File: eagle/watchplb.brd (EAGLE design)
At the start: 100 x 80 mm, 99 parts, among them IC1 SAM-M8Q, IC2 BM70BLES1FC2-0B03AA, Q1 8MHz / LFXTAL020423Reel, Q3 DMN3023L-7, U1 MCP111-XXXXX/TO, U2 STM32L073RZ, U3 MCP2200-I/SS

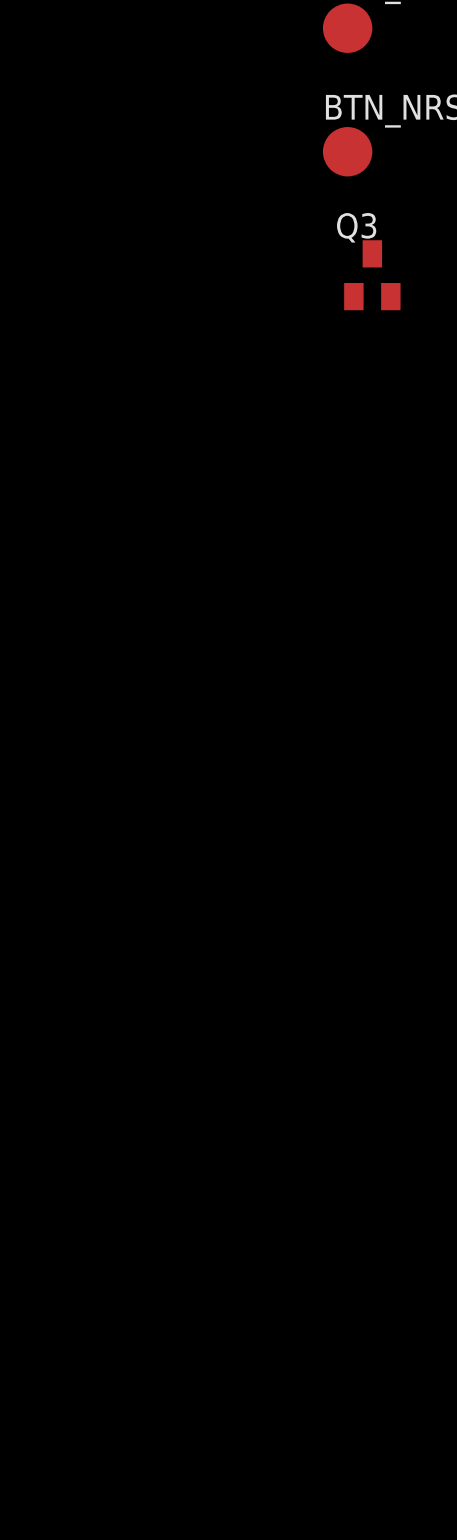
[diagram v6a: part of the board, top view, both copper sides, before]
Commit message: added VCOM usb port with protection
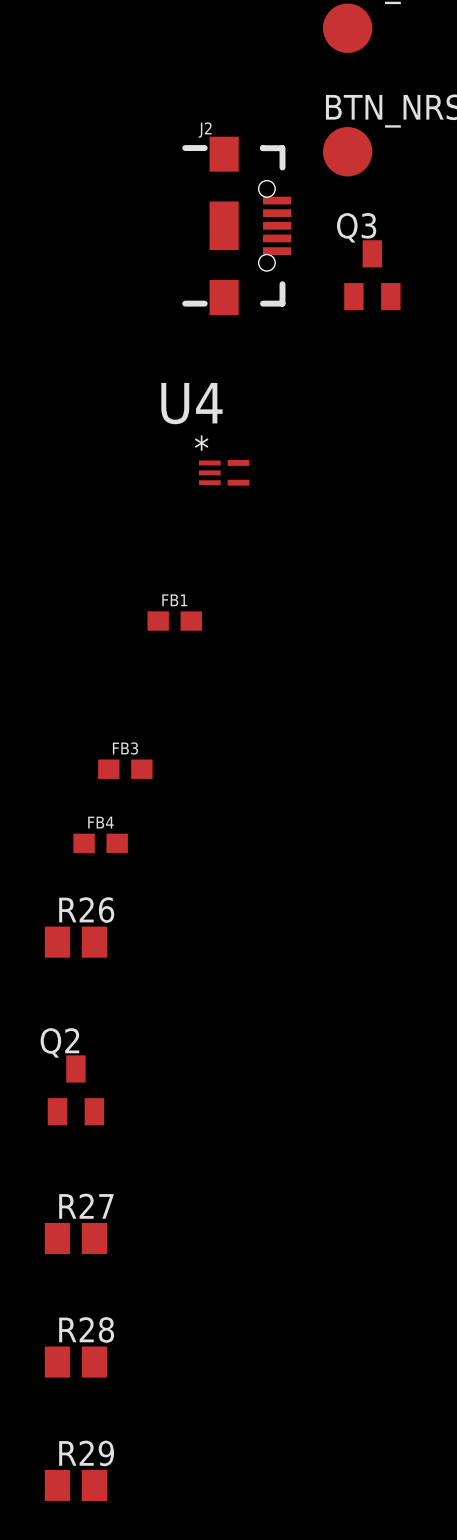
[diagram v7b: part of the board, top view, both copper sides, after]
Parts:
- added FB1, FB3, FB4: BLM18PG300SN1D, SparkFun-Coils:0603
- added J2: (no value), SparkFun-Connectors:USB-B-MICRO-SMD
- added Q2: BC817-25SMD, transistor-npn:SOT23-BEC
- added R26: 100k, resistor:M0805
- added R27, R28, R29: x, resistor:M0805
- added U4: TPD3E001DRLR, Texas Instruments_By_element14_Batch_1:SOT50P160X60-5N
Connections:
- new net N$29: FB4.2, J2.SHIELD1, J2.SHIELD2, J2.SHIELD3
- new net N$30: FB3.2, J2.GND
- new net N$31: FB1.1, J2.VBUS
- new net N$32: J2.ID, R26.1, U4.4
- new net N$35: Q2.E, R27.1
- new net N$36: Q2.B, R28.1, R29.2
- new net USB_DATA_NEG: J2.D-, U4.2
- new net USB_DATA_POS: J2.D+, R27.2, U4.1
- net +3V3: now also Q2.C
- net +5V: now also FB1.2, R29.1, U4.5
- net GND: now also FB3.1, FB4.1, R26.2, R28.2, U4.3
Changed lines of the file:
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@@
 </element>
 <element name="Q3" library="transistor-small-signal" package="SOT23" value="DMN3023L-7 " x="-120.65" y="-605.79"/>
+<element name="J2" library="SparkFun-Connectors" package="USB-B-MICRO-SMD" value="" x="-128.27" y="-603.25">
+<attribute name="PROD_ID" value="CONN-11752" x="-128.27" y="-603.25" size="1.778" layer="27" display="off"/>
+</element>
+<element name="U4" library="Texas Instruments_By_element14_Batch_1" package="SOT50P160X60-5N" value="TPD3E001DRLR" x="-128.27" y="-615.95">
+<attribute name="PACKAGE" value="SOT-5" x="-128.27" y="-615.95" size="1.778" layer="27" display="off"/>
+<attribute name="OC_NEWARK" value="41M5842" x="-128.27" y="-615.95" size="1.778" layer="27" display="off"/>
+<attribute name="MPN" value="TPD3E001DRLR" x="-128.27" y="-615.95" size="1.778" layer="27" display="off"/>
+<attribute name="SUPPLIER" value="Texas Instruments" x="-128.27" y="-615.95" size="1.778" layer="27" display="off"/>
+<attribute name="OC_FARNELL" value="1603422" x="-128.27" y="-615.95" size="1.778" layer="27" display="off"/>
+</element>
+<element name="FB1" library="SparkFun-Coils" package="0603" value="BLM18PG300SN1D" x="-130.81" y="-623.57">
+<attribute name="PROD_ID" value="NDUC-13805" x="-130.81" y="-623.57" size="1.778" layer="27" display="off"/>
+</element>
+<element name="FB3" library="SparkFun-Coils" package="0603" value="BLM18PG300SN1D" x="-133.35" y="-631.19">
+<attribute name="PROD_ID" value="NDUC-13805" x="-133.35" y="-631.19" size="1.778" layer="27" display="off"/>
+</element>
+<element name="FB4" library="SparkFun-Coils" package="0603" value="BLM18PG300SN1D" x="-134.62" y="-635">
+<attribute name="PROD_ID" value="NDUC-13805" x="-134.62" y="-635" size="1.778" layer="27" display="off"/>
+</element>
+<element name="R26" library="resistor" package="M0805" value="100k" x="-135.89" y="-640.08"/>
+<element name="Q2" library="transistor-npn" package="SOT23-BEC" value="BC817-25SMD" x="-135.89" y="-647.7"/>
+<element name="R27" library="resistor" package="M0805" value="x" x="-135.89" y="-655.32"/>
+<element name="R28" library="resistor" package="M0805" value="x" x="-135.89" y="-661.67"/>
+<element name="R29" library="resistor" package="M0805" value="x" x="-135.89" y="-668.02"/>
 </elements>
 <signals>
@@
 <contactref element="U2" pad="19"/>
 <contactref element="3V3" pad="TP"/>
+<contactref element="Q2" pad="C"/>
 <wire x1="-74.08" y1="-193.04" x2="-67.31" y2="-185.42" width="0" layer="19" extent="1-1"/>
 <wire x1="-81.09" y1="-216.13" x2="-74.08" y2="-193.04" width="0" layer="19" extent="1-1"/>
@@
 <wire x1="-68.39" y1="-139.93" x2="-67.31" y2="-185.42" width="0" layer="19" extent="1-1"/>
 <wire x1="-76.39" y1="-136.93" x2="-68.39" y2="-139.93" width="0" layer="19" extent="1-1"/>
-<wire x1="-64.45" y1="-104.14" x2="-68.39" y2="-139.93" width="0" layer="19" extent="1-1"/>
+<wire x1="-64.45" y1="-104.14" x2="-76.39" y2="-136.93" width="0" layer="19" extent="1-1"/>
 <wire x1="-68.39" y1="-101.83" x2="-64.45" y2="-104.14" width="0" layer="19" extent="1-1"/>
 <wire x1="-76.39" y1="-98.83" x2="-68.39" y2="-101.83" width="0" layer="19" extent="1-1"/>
@@
 <wire x1="54.86" y1="46.35" x2="46.36" y2="51.05" width="0" layer="19" extent="16-16"/>
 <wire x1="54.86" y1="44.45" x2="54.86" y2="46.35" width="0" layer="19" extent="16-16"/>
-<wire x1="-88.7984" y1="-263.184640625" x2="-89.09" y2="-213.13" width="0" layer="19" extent="1-1"/>
+<wire x1="-88.7984" y1="-263.184640625" x2="-81.09" y2="-216.13" width="0" layer="19" extent="1-1"/>
 <wire x1="-89.09" y1="-272.82" x2="-88.7984" y2="-263.184640625" width="0" layer="19" extent="1-1"/>
 <wire x1="-81.09" y1="-275.82" x2="-89.09" y2="-272.82" width="0" layer="19" extent="1-1"/>
-<wire x1="-111.44" y1="-370.84" x2="-89.09" y2="-272.82" width="0" layer="19" extent="1-1"/>
+<wire x1="-111.44" y1="-370.84" x2="-81.09" y2="-275.82" width="0" layer="19" extent="1-1"/>
 <wire x1="-111.44" y1="-377.19" x2="-111.44" y2="-370.84" width="0" layer="19" extent="1-1"/>
 <wire x1="-121.92" y1="-521.97" x2="-111.44" y2="-377.19" width="0" layer="19" extent="1-1"/>
+<wire x1="-135.89" y1="-646.6" x2="-121.92" y2="-521.97" width="0" layer="19" extent="1-1"/>
 </signal>
 <signal name="GPS_RXD">
@@
 <contactref element="R25" pad="2"/>
 <contactref element="Q3" pad="2"/>
+<contactref element="FB3" pad="1"/>
+<contactref element="FB4" pad="1"/>
+<contactref element="R26" pad="2"/>
+<contactref element="U4" pad="3"/>
+<contactref element="R28" pad="2"/>
 <wire x1="-74.08" y1="-166.37" x2="-74.08" y2="-172.72" width="0" layer="19" extent="1-1"/>
 <wire x1="-74.93" y1="-185.42" x2="-74.08" y2="-172.72" width="0" layer="19" extent="1-1"/>
@@
 <wire x1="44.46" y1="37.85" x2="41.66" y2="40.65" width="0" layer="19" extent="16-16"/>
 <wire x1="-119.7" y1="-606.89" x2="-119.7" y2="-401.32" width="0" layer="19" extent="1-1"/>
+<wire x1="-129.0066" y1="-616.458" x2="-119.7" y2="-606.89" width="0" layer="19" extent="1-1"/>
+<wire x1="-134.2" y1="-631.19" x2="-129.0066" y2="-616.458" width="0" layer="19" extent="1-1"/>
+<wire x1="-135.47" y1="-635" x2="-134.2" y2="-631.19" width="0" layer="19" extent="1-1"/>
+<wire x1="-134.94" y1="-640.08" x2="-135.47" y2="-635" width="0" layer="19" extent="1-1"/>
+<wire x1="-134.94" y1="-661.67" x2="-134.94" y2="-640.08" width="0" layer="19" extent="1-1"/>
 </signal>
 <signal name="BT_NRST">
@@
 <contactref element="U3" pad="1"/>
 <contactref element="USB_5V" pad="TP"/>
+<contactref element="FB1" pad="2"/>
+<contactref element="U4" pad="5"/>
+<contactref element="R29" pad="1"/>
+<wire x1="-127.5334" y1="-615.442" x2="-129.96" y2="-623.57" width="0" layer="19" extent="1-1"/>
+<wire x1="-136.84" y1="-668.02" x2="-129.96" y2="-623.57" width="0" layer="19" extent="1-1"/>
+<wire x1="-121.92" y1="-541.02" x2="-127.5334" y2="-615.442" width="0" layer="19" extent="1-1"/>
+<wire x1="-98.875" y1="-353.03" x2="-121.92" y2="-541.02" width="0" layer="19" extent="1-1"/>
 <wire x1="-88.7984" y1="-261.23391875" x2="-98.875" y2="-353.03" width="0" layer="19" extent="1-1"/>
-<wire x1="-121.92" y1="-541.02" x2="-98.875" y2="-353.03" width="0" layer="19" extent="1-1"/>
 </signal>
 <signal name="SWD_RX">
@@
 <wire x1="-52.74" y1="-45.93" x2="-122.5" y2="-557.53" width="0" layer="19" extent="1-1"/>
 </signal>
+<signal name="N$29">
+<contactref element="J2" pad="SHIELD2"/>
+<contactref element="J2" pad="SHIELD3"/>
+<contactref element="J2" pad="SHIELD1"/>
+<contactref element="FB4" pad="2"/>
+<wire x1="-128.27" y1="-603.25" x2="-128.27" y2="-606.935" width="0" layer="19" extent="1-1"/>
+<wire x1="-128.27" y1="-599.565" x2="-128.27" y2="-603.25" width="0" layer="19" extent="1-1"/>
+<wire x1="-133.77" y1="-635" x2="-128.27" y2="-606.935" width="0" layer="19" extent="1-1"/>
+</signal>
+<signal name="N$30">
+<contactref element="J2" pad="GND"/>
+<contactref element="FB3" pad="2"/>
+<wire x1="-132.5" y1="-631.19" x2="-125.545" y2="-604.55" width="0" layer="19" extent="1-1"/>
+</signal>
+<signal name="N$32">
+<contactref element="J2" pad="ID"/>
+<contactref element="R26" pad="1"/>
+<contactref element="U4" pad="4"/>
+<wire x1="-125.545" y1="-603.9" x2="-127.5334" y2="-616.458" width="0" layer="19" extent="1-1"/>
+<wire x1="-136.84" y1="-640.08" x2="-127.5334" y2="-616.458" width="0" layer="19" extent="1-1"/>
+</signal>
+<signal name="USB_DATA_POS">
+<contactref element="J2" pad="D+"/>
+<contactref element="U4" pad="1"/>
+<contactref element="R27" pad="2"/>
+<wire x1="-125.545" y1="-603.25" x2="-129.0066" y2="-615.442" width="0" layer="19" extent="1-1"/>
+<wire x1="-134.94" y1="-655.32" x2="-129.0066" y2="-615.442" width="0" layer="19" extent="1-1"/>
+</signal>
+<signal name="USB_DATA_NEG">
+<contactref element="J2" pad="D-"/>
+<contactref element="U4" pad="2"/>
+<wire x1="-125.545" y1="-602.6" x2="-129.0066" y2="-615.95" width="0" layer="19" extent="1-1"/>
+</signal>
+<signal name="N$31">
+<contactref element="J2" pad="VBUS"/>
+<contactref element="FB1" pad="1"/>
+<wire x1="-125.545" y1="-601.95" x2="-131.66" y2="-623.57" width="0" layer="19" extent="1-1"/>
+</signal>
+<signal name="N$35">
+<contactref element="Q2" pad="E"/>
+<contactref element="R27" pad="1"/>
+<wire x1="-134.94" y1="-648.8" x2="-136.84" y2="-655.32" width="0" layer="19" extent="1-1"/>
+</signal>
+<signal name="N$36">
+<contactref element="Q2" pad="B"/>
+<contactref element="R29" pad="2"/>
+<contactref element="R28" pad="1"/>
+<wire x1="-136.84" y1="-661.67" x2="-134.94" y2="-668.02" width="0" layer="19" extent="1-1"/>
+<wire x1="-136.84" y1="-648.8" x2="-136.84" y2="-661.67" width="0" layer="19" extent="1-1"/>
+</signal>
 </signals>

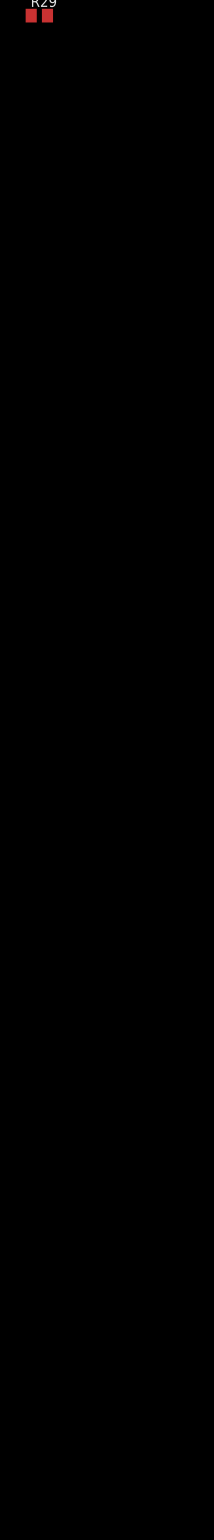
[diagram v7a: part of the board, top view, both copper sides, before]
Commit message: added RF transmitter (amp still missing) and generated new pdf of schematic for tobi
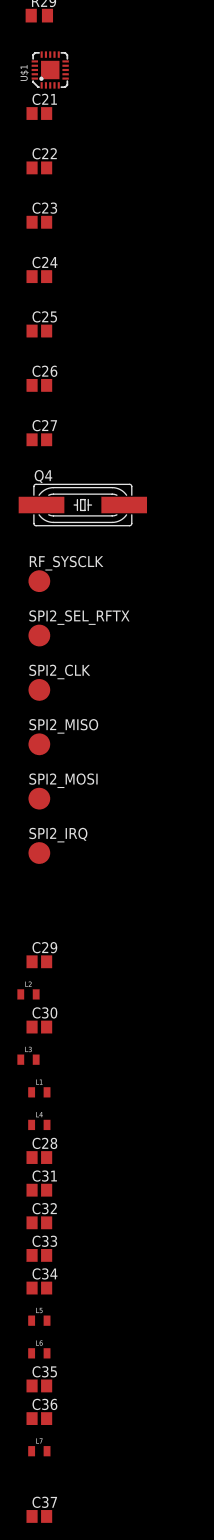
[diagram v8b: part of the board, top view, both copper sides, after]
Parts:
- added C21, C22, C23, C24: 100nF, resistor:C0805
- added C25, C26: 27pF, resistor:C0805
- added C27: 1uF, resistor:C0805
- added C28, C29, C30, C31, C32, C33, C34, C35, C36, C37: (no value), resistor:C0805
- added L1, L2, L3, L4, L5, L6, L7: (no value), SparkFun-Coils:0805
- added Q4: 16MHz_LFXTAL051370Reel, adafruit:HC49UP
- added RF_SYSCLK, SPI2_CLK, SPI2_IRQ, SPI2_MISO, SPI2_MOSI, SPI2_SEL_RFTX: PTR1B2,54, testpad:B2,54
- added U$1: AX5031, Hick:QFN20
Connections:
- new net INT_POWER: C21.2, C22.2, C23.2, C25.2, C26.2, C27.2, C29.2, C30.1, L2.1, L3.2, U$1.1, U$1.17, U$1.4
- new net N$33: Q4.2, U$1.19
- new net N$34: Q4.1, U$1.20
- new net N$37: RF_SYSCLK.TP, U$1.7
- new net N$38: C24.2, U$1.15
- new net N$39: C28.1, L4.1
- new net N$40: C31.1, L1.1
- new net N$41: C29.1, L1.2, L2.2, U$1.3
- new net N$42: C31.2, C32.2, C34.2, L6.1
- new net N$43: C28.2, C33.1, C35.2, L5.2
- new net N$44: C30.2, L3.1, L4.2, U$1.2
- new net N$45: C35.1, C36.2, L6.2, L7.1
- new net RF_SIGNAL: C37.2, L7.2
- new net SPI2_CLK: SPI2_CLK.TP, U$1.9, U2.29
- new net SPI2_IRQ: SPI2_IRQ.TP, U$1.14, U2.8
- new net SPI2_MISO: SPI2_MISO.TP, U$1.10, U2.10
- new net SPI2_MOSI: SPI2_MOSI.TP, U$1.12, U2.11
- new net SPI2_SEL_RFTX: SPI2_SEL_RFTX.TP, U$1.8, U2.9
- net GND: now also C21.1, C22.1, C23.1, C24.1, C25.1, C26.1, C27.1, C32.1, C33.2, C34.1, C36.1, C37.1, L5.1, U$1.PAD
